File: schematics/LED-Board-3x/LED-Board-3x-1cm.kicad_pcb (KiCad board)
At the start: 2 copper layers, 10 x 48 mm, 5 parts, among them P1 CONN_02X04

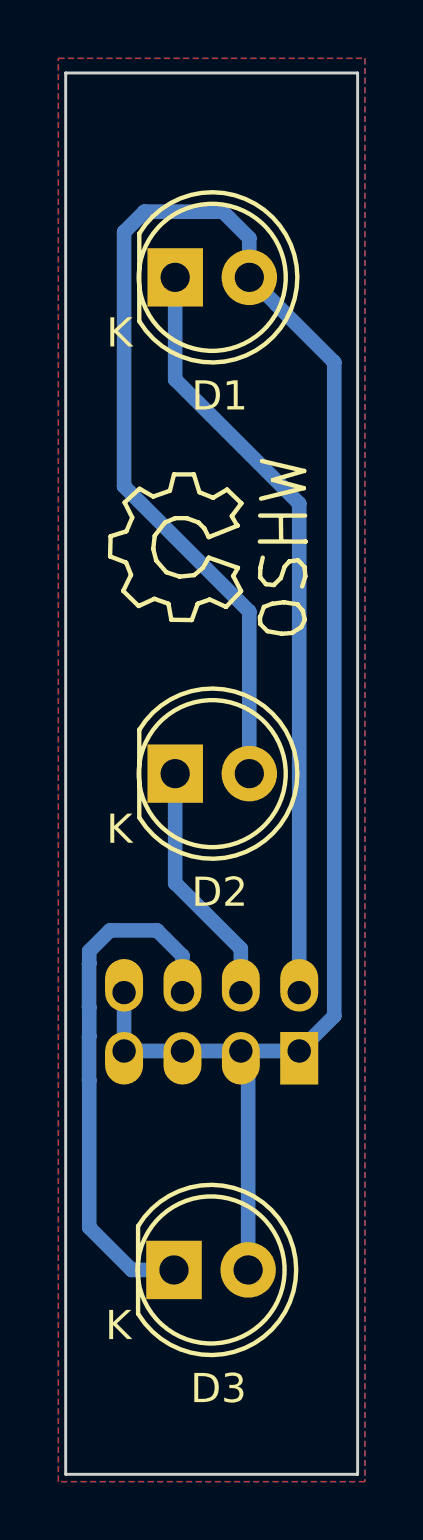
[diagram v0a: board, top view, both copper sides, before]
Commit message: schematics: update LED connections, use 4x resistor arrays
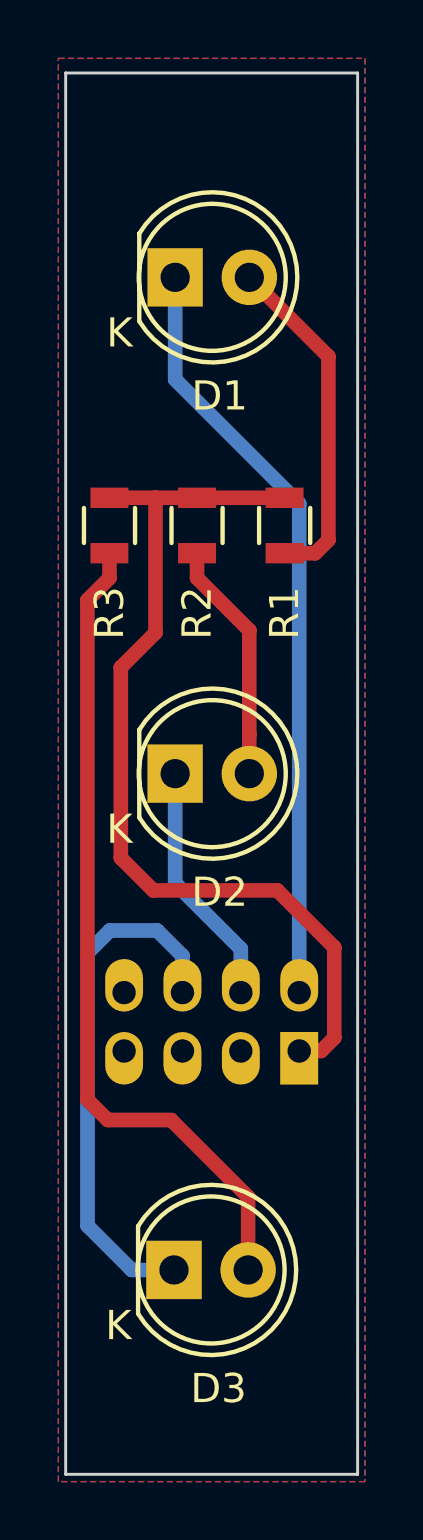
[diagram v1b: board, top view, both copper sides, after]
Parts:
- removed REF**: Symbol_OSHW-Logo_SilkScreen, Symbols:Symbol_OSHW-Logo_SilkScreen
- added R1: 220, Resistors_SMD:R_0805, F.Cu at (125.0, 68.0)
- added R2: 220, Resistors_SMD:R_0805, F.Cu at (122.0, 68.0)
- added R3: 220, Resistors_SMD:R_0805, F.Cu at (119.0, 68.0)
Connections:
- D1 pad 2: +3V3 -> Net-(D1-Pad2)
- D2 pad 2: +3V3 -> Net-(D2-Pad2)
- D3 pad 2: +3V3 -> Net-(D3-Pad2)
- P1 pad 3: +3V3 -> (no net)
- P1 pad 5: +3V3 -> (no net)
- P1 pad 7: +3V3 -> (no net)
- P1 pad 8: +3V3 -> (no net)
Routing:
- net +3V3: track 70.5 -> 31.9 mm
- net Net-(D3-Pad2): track 0.00 -> 28.4 mm
- net Net-(D1-Pad2): track 0.00 -> 11.8 mm
- net Net-(D2-Pad2): track 0.00 -> 8.29 mm
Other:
- board text added: "DIλ LED board v0.9-1cm"
- board text removed: "DIλ Paris LED board v0.9-1cm"

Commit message: Schematics update
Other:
- board text added: "1"
- board text added: "DIλ LED board v0.9-3x-1cm"
- board text removed: "DIλ LED board v0.9-1cm"
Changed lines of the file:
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@@
-(kicad_pcb (version 4) (host pcbnew "(2015-08-06 BZR 6060)-product")
+(kicad_pcb (version 4) (host pcbnew "(2016-01-25 BZR 6514, Git a23e712)-product")
   (general
     (links 9)
-    (no_connects 1)
-    (area 117.449999 52.449999 127.550001 100.550001)
+    (no_connects 0)
+    (area 99.000001 45.4 129.15 100.750001)
     (thickness 1.6)
-    (drawings 7)
-    (tracks 43)
+    (drawings 8)
+    (tracks 40)
     (zones 0)
     (modules 7)
@@
   (page A4)
   (layers
-    (0 F.Cu signal)
-    (31 B.Cu signal)
+    (0 F.Cu signal hide)
+    (31 B.Cu signal hide)
     (32 B.Adhes user)
     (33 F.Adhes user)
@@
     (pad_drill 0.6)
     (pad_to_mask_clearance 0)
-    (aux_axis_origin 0 0)
+    (aux_axis_origin 117.5 100.5)
     (visible_elements FFFFFF7F)
     (pcbplotparams
-      (layerselection 0x00030_80000001)
-      (usegerberextensions false)
+      (layerselection 0x010f0_80000001)
+      (usegerberextensions true)
       (excludeedgelayer true)
       (linewidth 0.100000)
@@
       (viasonmask false)
       (mode 1)
-      (useauxorigin false)
+      (useauxorigin true)
       (hpglpennumber 1)
       (hpglpenspeed 20)
@@
       (plotvalue true)
       (plotinvisibletext false)
-      (padsonsilk false)
+      (padsonsilk true)
       (subtractmaskfromsilk false)
       (outputformat 1)
       (mirror false)
-      (drillshape 1)
+      (drillshape 0)
       (scaleselection 1)
-      (outputdirectory ""))
+      (outputdirectory LED-Board-3x-1cm))
   )
   (net 0 "")
@@
     (descr "Pin Header 2mm 4x2pin")
     (tags "CONN DEV")
-    (fp_text reference P1 (at 0 5 180) (layer B.SilkS) hide
+    (fp_text reference P1 (at 0 3.25 180) (layer B.SilkS)
       (effects (font (size 1 1) (thickness 0.15)) (justify mirror))
     )
@@
     )
   )
-  (gr_text "DIλ\nLED board\nv0.9-1cm" (at 122.5 68 90) (layer B.SilkS)
+  (gr_text 1 (at 125.5 88.25 270) (layer B.SilkS)
+    (effects (font (size 1.5 1.5) (thickness 0.3)) (justify mirror))
+  )
+  (gr_text "DIλ\nLED board\nv0.9-3x-1cm" (at 122.5 68 90) (layer B.SilkS)
     (effects (font (size 1.5 1.5) (thickness 0.2)) (justify mirror))
   )
@@
     (arrow2b (pts (xy 117.5 48.25) (xy 118.626504 47.663579)))
   )
-  (segment (start 123.5 86) (end 123.556097 86.056097) (width 0.5) (layer B.Cu) (net 0))
-  (segment (start 123.556097 86.056097) (end 123.732003 86.056097) (width 0.5) (layer B.Cu) (net 0))
-  (segment (start 123.732003 86.056097) (end 123.75 86.074094) (width 0.5) (layer B.Cu) (net 0))
   (segment (start 121.25 63) (end 121.25 59.5) (width 0.5) (layer B.Cu) (net 1))
   (segment (start 125.5 67.25) (end 121.25 63) (width 0.5) (layer B.Cu) (net 1))
